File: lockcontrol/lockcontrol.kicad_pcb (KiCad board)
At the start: 2 copper layers, 72.4 x 31.8 mm, 9 parts, among them J1 ButtonHeader, K1 G5Q-1A, U1 WeMos_D1_mini, U3 ULN2003, U4 Barrel_Jack_Switch, U5 Barrel_Jack_Switch

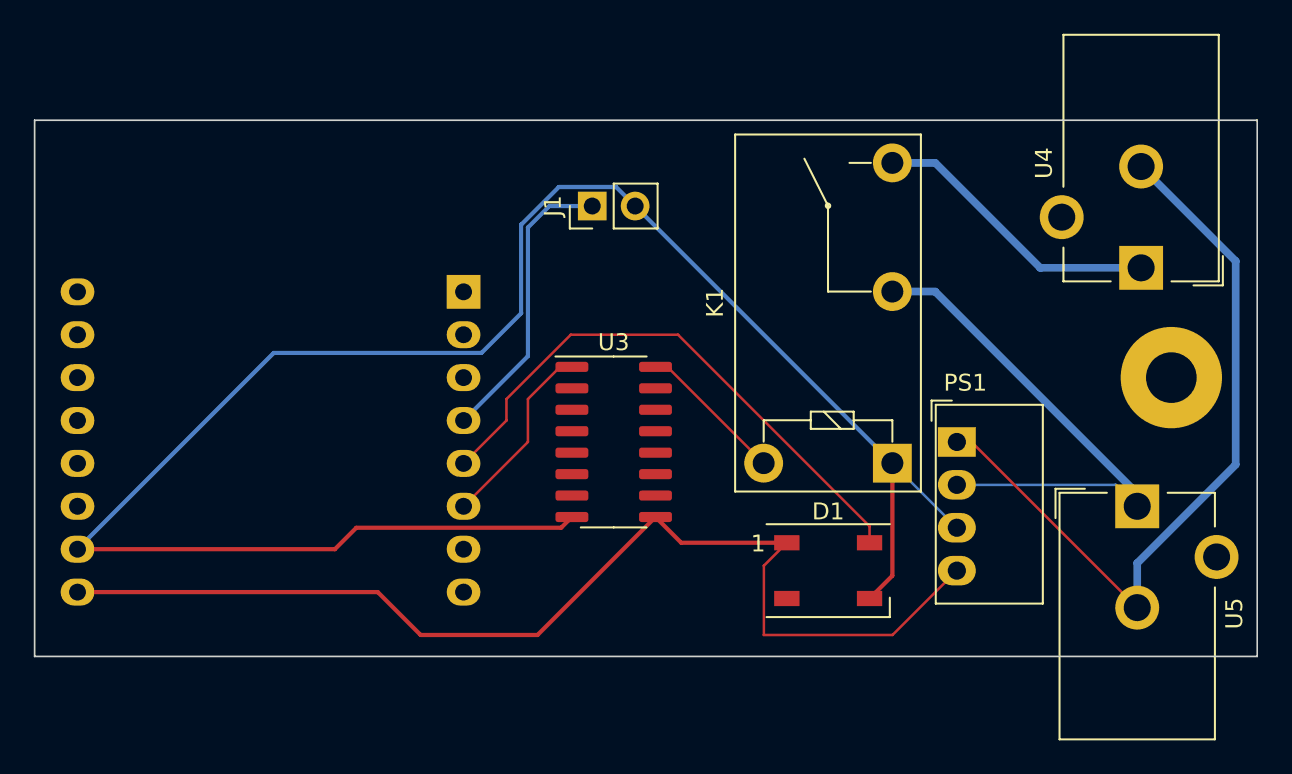
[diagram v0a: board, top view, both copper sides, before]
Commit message: update lock control footprints and esp pins
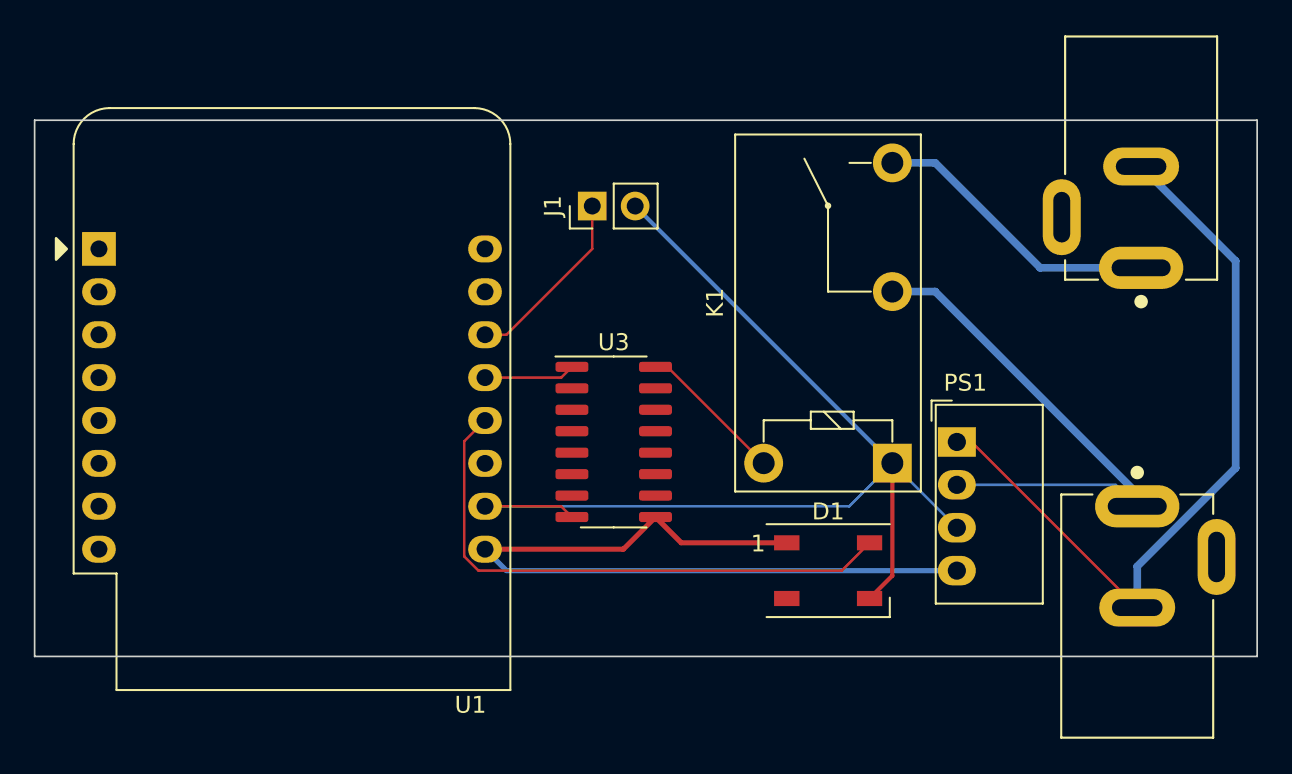
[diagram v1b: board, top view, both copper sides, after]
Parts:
- removed REF**: MountingHole_3mm_Pad, MountingHole:MountingHole_3mm_Pad
- U1: moved to F.Cu
- U4, U5: footprint Connector_BarrelJack:BarrelJack_CUI_PJ-102AH_Horizontal -> MyParts:CUI_PJ-002AH
- moved U1 21.7 mm to (104.1, 69.8), turned to 0 degrees
- turned U4 to 90 degrees
- turned U5 to -90 degrees
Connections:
- U1 pad 12: unconnected-(U1-Pad12) -> LED
- U1 pad 13: unconnected-(U1-Pad13) -> SWITCH
- U1 pad 14: unconnected-(U1-Pad14) -> BUTTON
- U1 pad 4: BUTTON -> unconnected-(U1-Pad4)
- U1 pad 5: LED -> unconnected-(U1-Pad5)
- U1 pad 6: SWITCH -> unconnected-(U1-Pad6)
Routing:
- net GND: track 111.0 -> 66.1 mm
- net 5V: track 65.6 -> 47.8 mm
- net BUTTON: track 17.3 -> 11.0 mm
- net SWITCH: track 11.3 -> 5.41 mm

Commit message: add mounting holes
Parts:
- added H1: MountingHole, MountingHole:MountingHole_2.1mm, F.Cu at (104.6, 65.5)
- added H2: MountingHole, MountingHole:MountingHole_2.1mm, F.Cu at (166.1, 77.7)
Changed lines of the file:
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@@
   (net 34 "12VGND")
   (net 35 "unconnected-(U1-Pad8)")
+  (footprint "MountingHole:MountingHole_2.1mm" (layer "F.Cu")
+    (at 104.648 65.532)
+    (descr "Mounting Hole 2.1mm, no annular")
+    (tags "mounting hole 2.1mm no annular")
+    (property "Sheetfile" "lockcontrol.kicad_sch")
+    (property "Sheetname" "")
+    (attr exclude_from_pos_files)
+    (fp_text reference "H1" (at 0 -3.2) (layer "F.SilkS") hide
+      (effects (font (size 1 1) (thickness 0.15)))
+    )
+    (fp_text value "MountingHole" (at 0 3.2) (layer "F.Fab") hide
+      (effects (font (size 1 1) (thickness 0.15)))
+    )
+    (fp_text user "${REFERENCE}" (at 0 0) (layer "F.Fab") hide
+      (effects (font (size 1 1) (thickness 0.15)))
+    )
+    (fp_circle (center 0 0) (end 2.1 0) (layer "Cmts.User") (width 0.15) (fill none))
+    (fp_circle (center 0 0) (end 2.35 0) (layer "F.CrtYd") (width 0.05) (fill none))
+    (pad "" np_thru_hole circle (at 0 0) (size 2.1 2.1) (drill 2.1) (layers *.Cu *.Mask))
+  )
   (footprint "Module:WEMOS_D1_mini_light" (layer "F.Cu")
     (at 104.14 69.85)
@@
     )
   )
+  (footprint "MountingHole:MountingHole_2.1mm" (layer "F.Cu")
+    (at 166.116 77.724)
+    (descr "Mounting Hole 2.1mm, no annular")
+    (tags "mounting hole 2.1mm no annular")
+    (property "Sheetfile" "lockcontrol.kicad_sch")
+    (property "Sheetname" "")
+    (attr exclude_from_pos_files)
+    (fp_text reference "H2" (at 0 -3.2) (layer "F.SilkS") hide
+      (effects (font (size 1 1) (thickness 0.15)))
+    )
+    (fp_text value "MountingHole" (at 0 3.2) (layer "F.Fab") hide
+      (effects (font (size 1 1) (thickness 0.15)))
+    )
+    (fp_text user "${REFERENCE}" (at 0 0) (layer "F.Fab") hide
+      (effects (font (size 1 1) (thickness 0.15)))
+    )
+    (fp_circle (center 0 0) (end 2.1 0) (layer "Cmts.User") (width 0.15) (fill none))
+    (fp_circle (center 0 0) (end 2.35 0) (layer "F.CrtYd") (width 0.05) (fill none))
+    (pad "" np_thru_hole circle (at 0 0) (size 2.1 2.1) (drill 2.1) (layers *.Cu *.Mask))
+  )
   (footprint "MyParts:CUI_PJ-002AH" (layer "F.Cu")

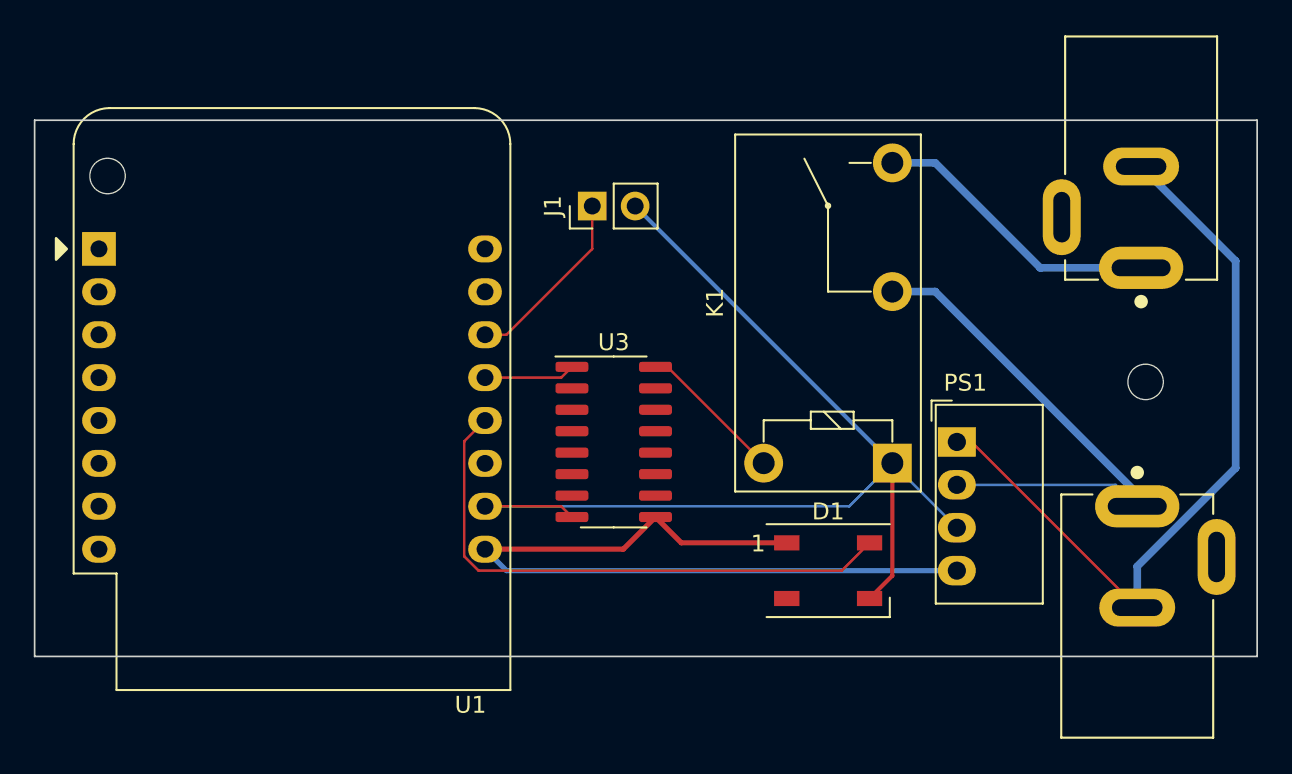
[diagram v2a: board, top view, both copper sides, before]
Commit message: mounting holes
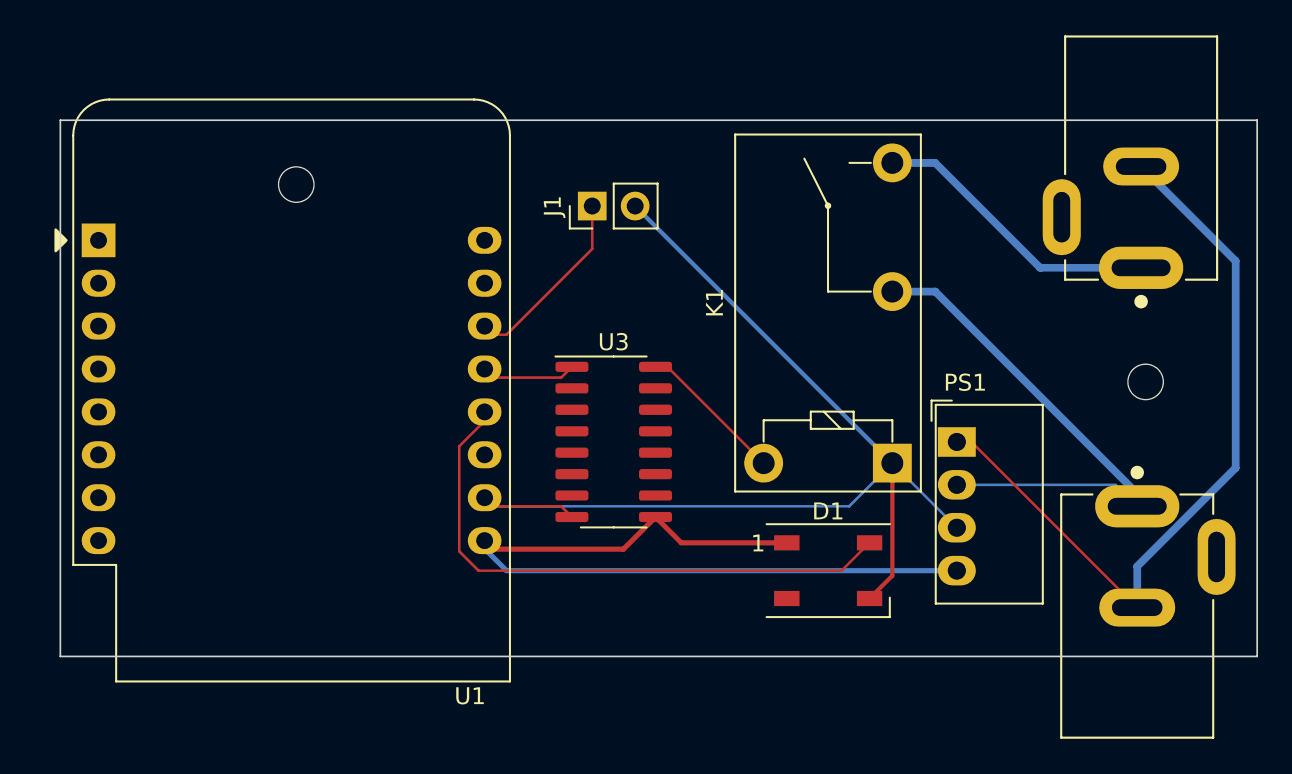
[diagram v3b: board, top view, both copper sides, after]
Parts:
- moved H1 11.2 mm to (115.8, 66.0)
- moved U1 0.51 mm to (104.1, 69.3)
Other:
- board size 72.4 x 31.8 mm -> 70.9 x 31.8 mm
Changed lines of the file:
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@@
   (net 35 "unconnected-(U1-Pad8)")
   (footprint "MountingHole:MountingHole_2.1mm" (layer "F.Cu")
-    (at 104.648 65.532)
+    (at 115.824 66.04)
     (descr "Mounting Hole 2.1mm, no annular")
     (tags "mounting hole 2.1mm no annular")
@@
   )
   (footprint "Module:WEMOS_D1_mini_light" (layer "F.Cu")
-    (at 104.14 69.85)
+    (at 104.117 69.342)
     (descr "16-pin module, column spacing 22.86 mm (900 mils), https://wiki.wemos.cc/products:d1:d1_mini, https://c1.staticflickr.com/1/734/31400410271_f278b087db_z.jpg")
     (tags "ESP8266 WiFi microcontroller")
@@
     )
   )
-  (gr_line (start 100.33 93.98) (end 172.72 93.98) (layer "Edge.Cuts") (width 0.1))
-  (gr_line (start 172.72 62.23) (end 100.33 62.23) (layer "Edge.Cuts") (width 0.1))
+  (gr_line (start 101.854 93.98) (end 172.72 93.98) (layer "Edge.Cuts") (width 0.1))
+  (gr_line (start 172.72 62.23) (end 101.854 62.23) (layer "Edge.Cuts") (width 0.1))
   (gr_line (start 172.72 93.98) (end 172.72 62.23) (layer "Edge.Cuts") (width 0.1))
-  (gr_line (start 100.33 62.23) (end 100.33 93.98) (layer "Edge.Cuts") (width 0.1))
+  (gr_line (start 101.854 62.23) (end 101.854 93.98) (layer "Edge.Cuts") (width 0.1))
   (segment (start 137.095 85.725) (end 138.62 87.25) (width 0.3048) (layer "F.Cu") (net 4))
   (segment (start 127 87.63) (end 135.19 87.63) (width 0.3048) (layer "F.Cu") (net 4))
@@
   (segment (start 151.12 82.54) (end 151.12 82.535) (width 0.1524) (layer "B.Cu") (net 6))
   (segment (start 151.12 82.535) (end 148.565 85.09) (width 0.1524) (layer "B.Cu") (net 6))
+  (segment (start 125.476 87.76066) (end 126.61534 88.9) (width 0.1524) (layer "F.Cu") (net 8))
+  (segment (start 125.476 81.534) (end 125.476 87.76066) (width 0.1524) (layer "F.Cu") (net 8))
+  (segment (start 127 80.01) (end 125.476 81.534) (width 0.1524) (layer "F.Cu") (net 8))
   (segment (start 148.12 88.9) (end 149.77 87.25) (width 0.1524) (layer "F.Cu") (net 8))
-  (segment (start 125.7714 88.05606) (end 126.61534 88.9) (width 0.1524) (layer "F.Cu") (net 8))
-  (segment (start 125.7714 81.2386) (end 125.7714 88.05606) (width 0.1524) (layer "F.Cu") (net 8))
-  (segment (start 127 80.01) (end 125.7714 81.2386) (width 0.1524) (layer "F.Cu") (net 8))
   (segment (start 126.61534 88.9) (end 148.12 88.9) (width 0.1524) (layer "F.Cu") (net 8))
   (segment (start 128.27 74.93) (end 133.35 69.85) (width 0.1524) (layer "F.Cu") (net 9))
